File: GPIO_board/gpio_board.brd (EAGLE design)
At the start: 93.6 x 79 mm, 15 parts, among them J1 SWITCHES, J2 LED1, J3 LED2, Q1 IRF520, Q2 IRF520, Q3 IRF520, X1 PCI-E-164SLOT

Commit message: saving before autorouting
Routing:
- net N$24: track 2.54 -> 13.8 mm
- net N$23: track 2.54 -> 13.8 mm
- net N$22: track 2.54 -> 13.8 mm
- net N$21: track 2.54 -> 13.8 mm
- net N$17: track 2.54 -> 13.8 mm
- net N$16: track 2.54 -> 13.8 mm
- net N$15: track 2.54 -> 13.8 mm
- net N$14: track 2.54 -> 13.8 mm
- net N$20: track 2.54 -> 13.8 mm
- net N$19: track 2.54 -> 13.8 mm
- net N$18: track 2.54 -> 13.8 mm
- net N$13: track 29.0 -> 38.5 mm
- net N$25: track 28.2 -> 36.0 mm
- net N$26: track 27.5 -> 33.4 mm
- net N$27: track 26.8 -> 30.9 mm
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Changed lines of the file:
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@@
 <setting verticaltext="up"/>
 </settings>
-<grid distance="0.05" unitdist="inch" unit="inch" style="lines" multiple="1" display="yes" altdistance="0.005" altunitdist="inch" altunit="inch"/>
+<grid distance="0.005" unitdist="inch" unit="inch" style="lines" multiple="1" display="yes" altdistance="0.005" altunitdist="inch" altunit="inch"/>
 <layers>
 <layer number="1" name="Top" color="4" fill="1" visible="yes" active="yes"/>
@@
 <signal name="N$14">
 <contactref element="U$1" pad="23/A9"/>
-<wire x1="36.83" y1="43.18" x2="39.37" y2="43.18" width="0.4064" layer="1"/>
 <contactref element="U$2" pad="P$16"/>
-<wire x1="46.99" y1="52.07" x2="36.83" y2="43.18" width="0" layer="19" extent="1-1"/>
+<wire x1="36.83" y1="43.18" x2="38.1" y2="43.18" width="0.4064" layer="1"/>
+<wire x1="38.1" y1="43.18" x2="46.99" y2="52.07" width="0.4064" layer="1"/>
 </signal>
 <signal name="N$15">
 <contactref element="U$1" pad="22/A8"/>
-<wire x1="36.83" y1="40.64" x2="39.37" y2="40.64" width="0.4064" layer="1"/>
 <contactref element="U$2" pad="P$15"/>
-<wire x1="46.99" y1="49.53" x2="36.83" y2="40.64" width="0" layer="19" extent="1-1"/>
+<wire x1="36.83" y1="40.64" x2="38.1" y2="40.64" width="0.4064" layer="1"/>
+<wire x1="38.1" y1="40.64" x2="46.99" y2="49.53" width="0.4064" layer="1"/>
 </signal>
 <signal name="N$16">
 <contactref element="U$1" pad="21/A7"/>
-<wire x1="36.83" y1="38.1" x2="39.37" y2="38.1" width="0.4064" layer="1"/>
 <contactref element="U$2" pad="P$14"/>
-<wire x1="46.99" y1="46.99" x2="36.83" y2="38.1" width="0" layer="19" extent="1-1"/>
+<wire x1="46.99" y1="46.99" x2="38.1" y2="38.1" width="0.4064" layer="1"/>
+<wire x1="38.1" y1="38.1" x2="36.83" y2="38.1" width="0.4064" layer="1"/>
 </signal>
 <signal name="N$17">
 <contactref element="U$1" pad="20/A6"/>
-<wire x1="36.83" y1="35.56" x2="39.37" y2="35.56" width="0.4064" layer="1"/>
 <contactref element="U$2" pad="P$13"/>
-<wire x1="46.99" y1="44.45" x2="36.83" y2="35.56" width="0" layer="19" extent="1-1"/>
+<wire x1="36.83" y1="35.56" x2="38.1" y2="35.56" width="0.4064" layer="1"/>
+<wire x1="38.1" y1="35.56" x2="46.99" y2="44.45" width="0.4064" layer="1"/>
 </signal>
 <signal name="N$18">
 <contactref element="U$1" pad="19/A5"/>
-<wire x1="36.83" y1="33.02" x2="39.37" y2="33.02" width="0.4064" layer="1"/>
 <contactref element="U$2" pad="P$12"/>
-<wire x1="46.99" y1="41.91" x2="36.83" y2="33.02" width="0" layer="19" extent="1-1"/>
+<wire x1="36.83" y1="33.02" x2="38.1" y2="33.02" width="0.4064" layer="1"/>
+<wire x1="38.1" y1="33.02" x2="46.99" y2="41.91" width="0.4064" layer="1"/>
 </signal>
 <signal name="N$19">
 <contactref element="U$1" pad="18/A4"/>
-<wire x1="36.83" y1="30.48" x2="39.37" y2="30.48" width="0.4064" layer="1"/>
 <contactref element="U$2" pad="P$11"/>
-<wire x1="46.99" y1="39.37" x2="36.83" y2="30.48" width="0" layer="19" extent="1-1"/>
+<wire x1="36.83" y1="30.48" x2="38.1" y2="30.48" width="0.4064" layer="1"/>
+<wire x1="38.1" y1="30.48" x2="46.99" y2="39.37" width="0.4064" layer="1"/>
 </signal>
 <signal name="N$20">
 <contactref element="U$1" pad="17/A3"/>
-<wire x1="36.83" y1="27.94" x2="39.37" y2="27.94" width="0.4064" layer="1"/>
 <contactref element="U$2" pad="P$10"/>
-<wire x1="46.99" y1="36.83" x2="36.83" y2="27.94" width="0" layer="19" extent="1-1"/>
+<wire x1="36.83" y1="27.94" x2="38.1" y2="27.94" width="0.4064" layer="1"/>
+<wire x1="38.1" y1="27.94" x2="46.99" y2="36.83" width="0.4064" layer="1"/>
 </signal>
 <signal name="N$21">
 <contactref element="U$1" pad="16/A2"/>
-<wire x1="36.83" y1="25.4" x2="39.37" y2="25.4" width="0.4064" layer="1"/>
 <contactref element="U$2" pad="P$9"/>
-<wire x1="46.99" y1="34.29" x2="36.83" y2="25.4" width="0" layer="19" extent="1-1"/>
+<wire x1="36.83" y1="25.4" x2="38.1" y2="25.4" width="0.4064" layer="1"/>
+<wire x1="38.1" y1="25.4" x2="46.99" y2="34.29" width="0.4064" layer="1"/>
 </signal>
 <signal name="N$22">
 <contactref element="U$1" pad="15/A1"/>
-<wire x1="36.83" y1="22.86" x2="39.37" y2="22.86" width="0.4064" layer="1"/>
 <contactref element="U$2" pad="P$8"/>
-<wire x1="46.99" y1="31.75" x2="36.83" y2="22.86" width="0" layer="19" extent="1-1"/>
+<wire x1="36.83" y1="22.86" x2="38.1" y2="22.86" width="0.4064" layer="1"/>
+<wire x1="38.1" y1="22.86" x2="46.99" y2="31.75" width="0.4064" layer="1"/>
 </signal>
 <signal name="N$23">
 <contactref element="U$1" pad="14/A0"/>
-<wire x1="36.83" y1="20.32" x2="39.37" y2="20.32" width="0.4064" layer="1"/>
 <contactref element="U$2" pad="P$7"/>
-<wire x1="46.99" y1="29.21" x2="36.83" y2="20.32" width="0" layer="19" extent="1-1"/>
+<wire x1="36.83" y1="20.32" x2="38.1" y2="20.32" width="0.4064" layer="1"/>
+<wire x1="38.1" y1="20.32" x2="46.99" y2="29.21" width="0.4064" layer="1"/>
 </signal>
 <signal name="N$24">
 <contactref element="U$1" pad="13"/>
-<wire x1="36.83" y1="17.78" x2="39.37" y2="17.78" width="0.4064" layer="1"/>
 <contactref element="U$2" pad="P$6"/>
-<wire x1="46.99" y1="26.67" x2="36.83" y2="17.78" width="0" layer="19" extent="1-1"/>
+<wire x1="36.83" y1="17.78" x2="38.1" y2="17.78" width="0.4064" layer="1"/>
+<wire x1="38.1" y1="17.78" x2="46.99" y2="26.67" width="0.4064" layer="1"/>
 </signal>
 <signal name="N$13">
 <contactref element="U$1" pad="8"/>
+<contactref element="U$2" pad="P$5"/>
 <wire x1="21.59" y1="27.94" x2="33.02" y2="27.94" width="0.4064" layer="1"/>
 <wire x1="33.02" y1="27.94" x2="34.29" y2="26.67" width="0.4064" layer="1"/>
-<wire x1="34.29" y1="26.67" x2="34.29" y2="16.51" width="0.4064" layer="1"/>
-<wire x1="34.29" y1="16.51" x2="35.56" y2="15.24" width="0.4064" layer="1"/>
-<wire x1="35.56" y1="15.24" x2="39.37" y2="15.24" width="0.4064" layer="1"/>
-<contactref element="U$2" pad="P$5"/>
-<wire x1="46.99" y1="24.13" x2="34.29" y2="16.51" width="0" layer="19" extent="1-1"/>
+<wire x1="34.29" y1="26.67" x2="34.29" y2="17.78" width="0.4064" layer="1"/>
+<wire x1="34.29" y1="17.78" x2="35.56" y2="16.51" width="0.4064" layer="1"/>
+<wire x1="35.56" y1="16.51" x2="39.37" y2="16.51" width="0.4064" layer="1"/>
+<wire x1="39.37" y1="16.51" x2="46.99" y2="24.13" width="0.4064" layer="1"/>
 </signal>
 <signal name="N$25">
 <contactref element="U$1" pad="9"/>
+<contactref element="U$2" pad="P$4"/>
 <wire x1="21.59" y1="25.4" x2="31.75" y2="25.4" width="0.4064" layer="1"/>
 <wire x1="31.75" y1="25.4" x2="33.02" y2="24.13" width="0.4064" layer="1"/>
-<wire x1="33.02" y1="24.13" x2="33.02" y2="16.51" width="0.4064" layer="1"/>
-<wire x1="33.02" y1="16.51" x2="35.56" y2="13.97" width="0.4064" layer="1"/>
-<wire x1="35.56" y1="13.97" x2="40.64" y2="13.97" width="0.4064" layer="1"/>
-<contactref element="U$2" pad="P$4"/>
-<wire x1="46.99" y1="21.59" x2="21.59" y2="25.4" width="0" layer="19" extent="1-1"/>
+<wire x1="33.02" y1="24.13" x2="33.02" y2="17.78" width="0.4064" layer="1"/>
+<wire x1="33.02" y1="17.78" x2="35.56" y2="15.24" width="0.4064" layer="1"/>
+<wire x1="35.56" y1="15.24" x2="40.64" y2="15.24" width="0.4064" layer="1"/>
+<wire x1="40.64" y1="15.24" x2="46.99" y2="21.59" width="0.4064" layer="1"/>
 </signal>
 <signal name="N$26">
 <contactref element="U$1" pad="10"/>
+<contactref element="U$2" pad="P$3"/>
 <wire x1="21.59" y1="22.86" x2="30.48" y2="22.86" width="0.4064" layer="1"/>
 <wire x1="30.48" y1="22.86" x2="31.75" y2="21.59" width="0.4064" layer="1"/>
-<wire x1="31.75" y1="21.59" x2="31.75" y2="16.51" width="0.4064" layer="1"/>
-<wire x1="31.75" y1="16.51" x2="35.56" y2="12.7" width="0.4064" layer="1"/>
-<wire x1="35.56" y1="12.7" x2="41.91" y2="12.7" width="0.4064" layer="1"/>
-<contactref element="U$2" pad="P$3"/>
-<wire x1="46.99" y1="19.05" x2="21.59" y2="22.86" width="0" layer="19" extent="1-1"/>
+<wire x1="31.75" y1="21.59" x2="31.75" y2="17.78" width="0.4064" layer="1"/>
+<wire x1="31.75" y1="17.78" x2="35.56" y2="13.97" width="0.4064" layer="1"/>
+<wire x1="35.56" y1="13.97" x2="41.91" y2="13.97" width="0.4064" layer="1"/>
+<wire x1="41.91" y1="13.97" x2="46.99" y2="19.05" width="0.4064" layer="1"/>
 </signal>
 <signal name="N$27">
 <contactref element="U$1" pad="11"/>
+<contactref element="U$2" pad="P$2"/>
 <wire x1="21.59" y1="20.32" x2="29.21" y2="20.32" width="0.4064" layer="1"/>
 <wire x1="29.21" y1="20.32" x2="30.48" y2="19.05" width="0.4064" layer="1"/>
-<wire x1="30.48" y1="19.05" x2="30.48" y2="16.51" width="0.4064" layer="1"/>
-<wire x1="30.48" y1="16.51" x2="35.56" y2="11.43" width="0.4064" layer="1"/>
-<wire x1="35.56" y1="11.43" x2="43.18" y2="11.43" width="0.4064" layer="1"/>
-<contactref element="U$2" pad="P$2"/>
-<wire x1="46.99" y1="16.51" x2="21.59" y2="20.32" width="0" layer="19" extent="1-1"/>
+<wire x1="30.48" y1="19.05" x2="30.48" y2="17.78" width="0.4064" layer="1"/>
+<wire x1="30.48" y1="17.78" x2="35.56" y2="12.7" width="0.4064" layer="1"/>
+<wire x1="35.56" y1="12.7" x2="43.18" y2="12.7" width="0.4064" layer="1"/>
+<wire x1="43.18" y1="12.7" x2="46.99" y2="16.51" width="0.4064" layer="1"/>
 </signal>
 <signal name="N$28">
 <contactref element="U$1" pad="12"/>
-<wire x1="21.59" y1="17.78" x2="27.94" y2="17.78" width="0.4064" layer="1"/>
-<wire x1="27.94" y1="17.78" x2="35.56" y2="10.16" width="0.4064" layer="1"/>
-<wire x1="35.56" y1="10.16" x2="44.45" y2="10.16" width="0.4064" layer="1"/>
 <contactref element="U$2" pad="P$1"/>
-<wire x1="46.99" y1="13.97" x2="21.59" y2="17.78" width="0" layer="19" extent="1-1"/>
+<wire x1="21.59" y1="17.78" x2="29.21" y2="17.78" width="0.4064" layer="1"/>
+<wire x1="29.21" y1="17.78" x2="35.56" y2="11.43" width="0.4064" layer="1"/>
+<wire x1="35.56" y1="11.43" x2="44.45" y2="11.43" width="0.4064" layer="1"/>
+<wire x1="44.45" y1="11.43" x2="46.99" y2="13.97" width="0.4064" layer="1"/>
 </signal>
 <signal name="N$29">

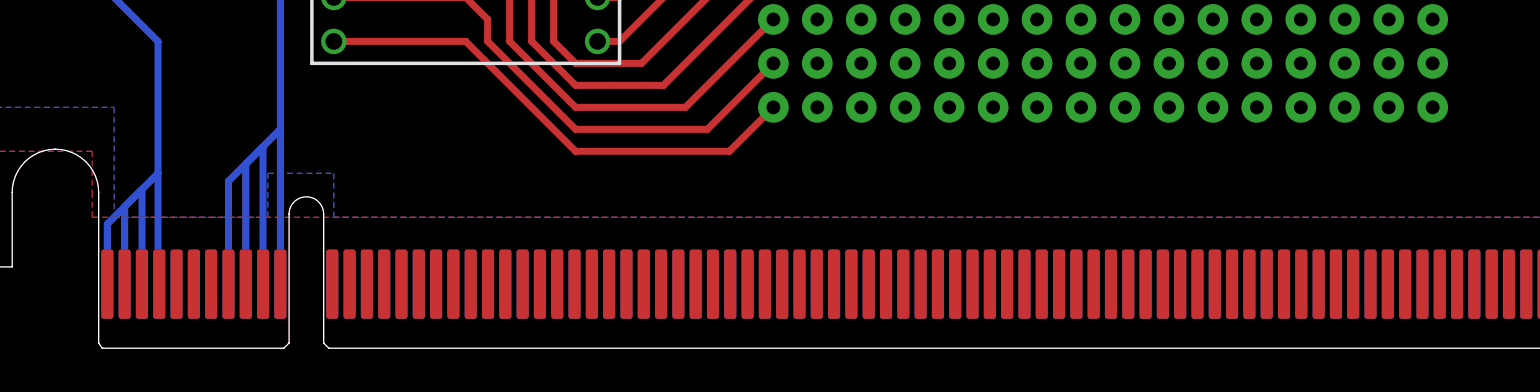
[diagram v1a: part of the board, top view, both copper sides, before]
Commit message: fixed traces from PCIe slot to proto_grid
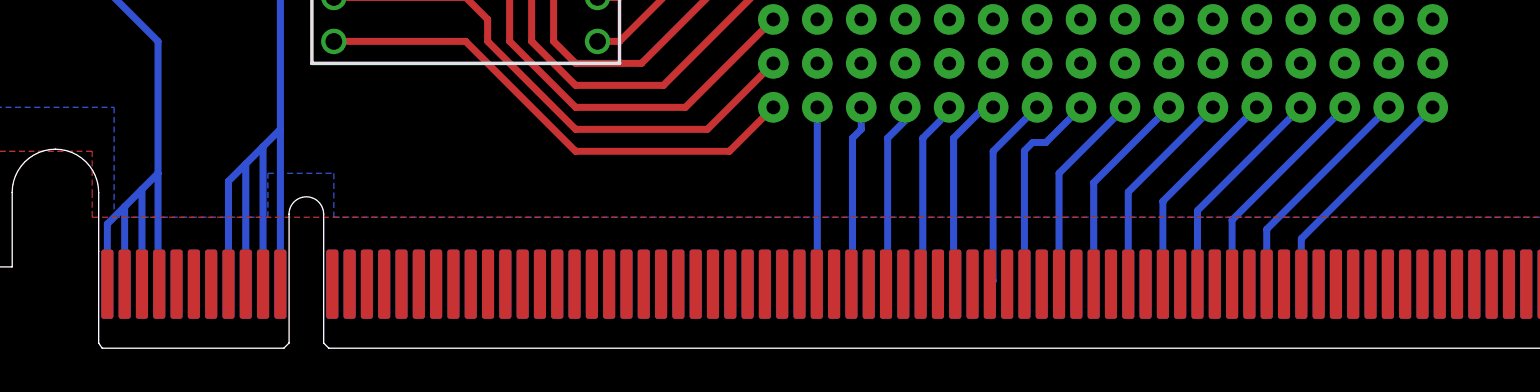
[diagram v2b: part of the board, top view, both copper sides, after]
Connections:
- net N$29: now also X1.A68; no longer X1.A54
- net N$30: now also X1.A66; no longer X1.A53
- net N$31: now also X1.A64; no longer X1.A52
- net N$32: now also X1.A62; no longer X1.A51
- net N$33: now also X1.A60; no longer X1.A50
- net N$34: now also X1.A58; no longer X1.A49
- net N$35: now also X1.A56; no longer X1.A48
- net N$36: now also X1.A54; no longer X1.A47
- net N$37: now also X1.A52; no longer X1.A46
- net N$38: now also X1.A50; no longer X1.A45
- net N$39: now also X1.A48; no longer X1.A44
- net N$40: now also X1.A46; no longer X1.A43
- net N$41: now also X1.A44; no longer X1.A42
- net N$42: now also X1.A42; no longer X1.A41
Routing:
- net N$29: track 0.00 -> 13.4 mm
- net N$30: track 0.00 -> 13.1 mm
- net N$31: track 0.00 -> 12.9 mm
- net N$32: track 0.00 -> 12.7 mm
- net N$33: track 0.00 -> 12.5 mm
- net N$34: track 0.00 -> 12.2 mm
- net N$35: track 0.00 -> 12.0 mm
- net N$37: track 0.00 -> 12.0 mm
- net N$36: track 0.00 -> 11.8 mm
- net N$39: track 0.00 -> 11.5 mm
- net N$38: track 0.00 -> 11.4 mm
- net N$40: track 0.00 -> 10.9 mm
- net N$41: track 0.00 -> 10.7 mm
- net N$42: track 0.00 -> 10.5 mm
- net N$43: track 0.00 -> 10.2 mm
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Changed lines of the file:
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@@
 <setting verticaltext="up"/>
 </settings>
-<grid distance="0.005" unitdist="inch" unit="inch" style="lines" multiple="1" display="yes" altdistance="0.005" altunitdist="inch" altunit="inch"/>
+<grid distance="0.01" unitdist="inch" unit="inch" style="lines" multiple="1" display="yes" altdistance="0.005" altunitdist="inch" altunit="inch"/>
 <layers>
 <layer number="1" name="Top" color="4" fill="1" visible="yes" active="yes"/>
@@
 <wire x1="17.78" y1="46.99" x2="21.59" y2="50.8" width="0.4064" layer="16"/>
 <wire x1="17.5" y1="3.75" x2="17.5" y2="11.7" width="0.4064" layer="16"/>
-<wire x1="17.5" y1="11.7" x2="18.14" y2="12.34" width="0.4064" layer="16"/>
-<wire x1="18.14" y1="12.34" x2="18.5" y2="12.7" width="0.4064" layer="16"/>
+<wire x1="17.5" y1="11.7" x2="18.5" y2="12.7" width="0.4064" layer="16"/>
 <wire x1="16.5" y1="3.75" x2="16.5" y2="10.7" width="0.4064" layer="16"/>
 <wire x1="16.5" y1="10.7" x2="17.5" y2="11.7" width="0.4064" layer="16"/>
 <wire x1="15.5" y1="3.75" x2="15.5" y2="9.7" width="0.4064" layer="16"/>
-<wire x1="15.5" y1="9.7" x2="17.5" y2="11.7" width="0.4064" layer="16"/>
+<wire x1="15.5" y1="9.7" x2="16.5" y2="10.7" width="0.4064" layer="16"/>
 <polygon width="0.4064" layer="1">
 <vertex x="-1.27" y="83.82"/>
@@
 <wire x1="9.5" y1="8.23" x2="10.5" y2="9.23" width="0.4064" layer="16"/>
 <wire x1="8.5" y1="3.75" x2="8.5" y2="7.23" width="0.4064" layer="16"/>
-<wire x1="8.5" y1="7.23" x2="10.5" y2="9.23" width="0.4064" layer="16"/>
+<wire x1="8.5" y1="7.23" x2="9.5" y2="8.23" width="0.4064" layer="16"/>
 </signal>
 <signal name="N$9">
@@
 <signal name="N$29">
 <contactref element="U$2" pad="P$225"/>
-<contactref element="X1" pad="A54"/>
-<wire x1="63.5" y1="3.75" x2="85.09" y2="13.97" width="0" layer="19" extent="16-16"/>
+<contactref element="X1" pad="A68"/>
+<wire x1="77.5" y1="3.75" x2="77.5" y2="6.38" width="0.4064" layer="16"/>
+<wire x1="77.5" y1="6.38" x2="85.09" y2="13.97" width="0.4064" layer="16"/>
 </signal>
 <signal name="N$30">
 <contactref element="U$2" pad="P$233"/>
-<contactref element="X1" pad="A53"/>
-<wire x1="62.5" y1="3.75" x2="82.55" y2="13.97" width="0" layer="19" extent="16-16"/>
+<contactref element="X1" pad="A66"/>
+<wire x1="75.5" y1="3.75" x2="75.5" y2="6.92" width="0.4064" layer="16"/>
+<wire x1="75.5" y1="6.92" x2="82.55" y2="13.97" width="0.4064" layer="16"/>
 </signal>
 <signal name="N$31">
 <contactref element="U$2" pad="P$193"/>
-<contactref element="X1" pad="A52"/>
-<wire x1="61.5" y1="3.75" x2="80.01" y2="13.97" width="0" layer="19" extent="16-16"/>
+<contactref element="X1" pad="A64"/>
+<wire x1="73.5" y1="3.75" x2="73.5" y2="7.46" width="0.4064" layer="16"/>
+<wire x1="73.5" y1="7.46" x2="80.01" y2="13.97" width="0.4064" layer="16"/>
 </signal>
 <signal name="N$32">
 <contactref element="U$2" pad="P$201"/>
-<contactref element="X1" pad="A51"/>
-<wire x1="60.5" y1="3.75" x2="77.47" y2="13.97" width="0" layer="19" extent="16-16"/>
+<contactref element="X1" pad="A62"/>
+<wire x1="71.5" y1="3.75" x2="71.5" y2="8" width="0.4064" layer="16"/>
+<wire x1="71.5" y1="8" x2="77.47" y2="13.97" width="0.4064" layer="16"/>
 </signal>
 <signal name="N$33">
 <contactref element="U$2" pad="P$161"/>
-<contactref element="X1" pad="A50"/>
-<wire x1="59.5" y1="3.75" x2="74.93" y2="13.97" width="0" layer="19" extent="16-16"/>
+<contactref element="X1" pad="A60"/>
+<wire x1="69.5" y1="3.75" x2="69.5" y2="8.54" width="0.4064" layer="16"/>
+<wire x1="69.5" y1="8.54" x2="74.93" y2="13.97" width="0.4064" layer="16"/>
 </signal>
 <signal name="N$34">
 <contactref element="U$2" pad="P$169"/>
-<contactref element="X1" pad="A49"/>
-<wire x1="58.5" y1="3.75" x2="72.39" y2="13.97" width="0" layer="19" extent="16-16"/>
+<contactref element="X1" pad="A58"/>
+<wire x1="67.5" y1="3.75" x2="67.5" y2="9.08" width="0.4064" layer="16"/>
+<wire x1="67.5" y1="9.08" x2="72.39" y2="13.97" width="0.4064" layer="16"/>
 </signal>
 <signal name="N$35">
 <contactref element="U$2" pad="P$129"/>
-<contactref element="X1" pad="A48"/>
-<wire x1="57.5" y1="3.75" x2="69.85" y2="13.97" width="0" layer="19" extent="16-16"/>
+<contactref element="X1" pad="A56"/>
+<wire x1="65.5" y1="3.75" x2="65.5" y2="9.62" width="0.4064" layer="16"/>
+<wire x1="65.5" y1="9.62" x2="69.85" y2="13.97" width="0.4064" layer="16"/>
 </signal>
 <signal name="N$36">
 <contactref element="U$2" pad="P$137"/>
-<contactref element="X1" pad="A47"/>
-<wire x1="56.5" y1="3.75" x2="67.31" y2="13.97" width="0" layer="19" extent="16-16"/>
+<contactref element="X1" pad="A54"/>
+<wire x1="63.5" y1="3.75" x2="63.5" y2="10.16" width="0.4064" layer="16"/>
+<wire x1="63.5" y1="10.16" x2="67.31" y2="13.97" width="0.4064" layer="16"/>
 </signal>
 <signal name="N$37">
 <contactref element="U$2" pad="P$97"/>
-<contactref element="X1" pad="A46"/>
-<wire x1="55.5" y1="3.75" x2="64.77" y2="13.97" width="0" layer="19" extent="16-16"/>
+<contactref element="X1" pad="A52"/>
+<wire x1="61.5" y1="3.75" x2="61.5" y2="11.462" width="0.4064" layer="16"/>
+<wire x1="61.5" y1="11.462" x2="61.976" y2="11.938" width="0.4064" layer="16"/>
+<wire x1="61.976" y1="11.938" x2="62.738" y2="11.938" width="0.4064" layer="16"/>
+<wire x1="62.738" y1="11.938" x2="64.77" y2="13.97" width="0.4064" layer="16"/>
 </signal>
 <signal name="N$38">
 <contactref element="U$2" pad="P$105"/>
-<contactref element="X1" pad="A45"/>
-<wire x1="54.5" y1="3.75" x2="62.23" y2="13.97" width="0" layer="19" extent="16-16"/>
+<contactref element="X1" pad="A50"/>
+<wire x1="62.23" y1="13.97" x2="59.69" y2="11.43" width="0.4064" layer="16"/>
+<wire x1="59.69" y1="11.43" x2="59.69" y2="3.94" width="0.4064" layer="16"/>
+<wire x1="59.69" y1="3.94" x2="59.5" y2="3.75" width="0.4064" layer="16"/>
 </signal>
 <signal name="N$39">
 <contactref element="U$2" pad="P$65"/>
-<contactref element="X1" pad="A44"/>
-<wire x1="53.5" y1="3.75" x2="59.69" y2="13.97" width="0" layer="19" extent="16-16"/>
+<contactref element="X1" pad="A48"/>
+<wire x1="59.69" y1="13.97" x2="59.182" y2="13.97" width="0.4064" layer="16"/>
+<wire x1="59.182" y1="13.97" x2="57.404" y2="12.192" width="0.4064" layer="16"/>
+<wire x1="57.404" y1="12.192" x2="57.404" y2="3.846" width="0.4064" layer="16"/>
+<wire x1="57.404" y1="3.846" x2="57.5" y2="3.75" width="0.4064" layer="16"/>
 </signal>
 <signal name="N$40">
 <contactref element="U$2" pad="P$73"/>
-<contactref element="X1" pad="A43"/>
-<wire x1="52.5" y1="3.75" x2="57.15" y2="13.97" width="0" layer="19" extent="16-16"/>
+<contactref element="X1" pad="A46"/>
+<wire x1="57.15" y1="13.97" x2="57.15" y2="13.716" width="0.4064" layer="16"/>
+<wire x1="57.15" y1="13.716" x2="55.626" y2="12.192" width="0.4064" layer="16"/>
+<wire x1="55.626" y1="12.192" x2="55.626" y2="3.876" width="0.4064" layer="16"/>
+<wire x1="55.626" y1="3.876" x2="55.5" y2="3.75" width="0.4064" layer="16"/>
 </signal>
 <signal name="N$41">
 <contactref element="U$2" pad="P$33"/>
-<contactref element="X1" pad="A42"/>
-<wire x1="51.5" y1="3.75" x2="54.61" y2="13.97" width="0" layer="19" extent="16-16"/>
+<contactref element="X1" pad="A44"/>
+<wire x1="54.61" y1="13.97" x2="54.61" y2="13.208" width="0.4064" layer="16"/>
+<wire x1="54.61" y1="13.208" x2="53.594" y2="12.192" width="0.4064" layer="16"/>
+<wire x1="53.594" y1="12.192" x2="53.594" y2="3.844" width="0.4064" layer="16"/>
+<wire x1="53.594" y1="3.844" x2="53.5" y2="3.75" width="0.4064" layer="16"/>
 </signal>
 <signal name="N$42">
 <contactref element="U$2" pad="P$41"/>
-<contactref element="X1" pad="A41"/>
-<wire x1="50.5" y1="3.75" x2="52.07" y2="13.97" width="0" layer="19" extent="16-16"/>
+<contactref element="X1" pad="A42"/>
+<wire x1="52.07" y1="13.97" x2="52.07" y2="12.7" width="0.4064" layer="16"/>
+<wire x1="52.07" y1="12.7" x2="51.562" y2="12.192" width="0.4064" layer="16"/>
+<wire x1="51.562" y1="12.192" x2="51.562" y2="3.812" width="0.4064" layer="16"/>
+<wire x1="51.562" y1="3.812" x2="51.5" y2="3.75" width="0.4064" layer="16"/>
 </signal>
 <signal name="N$43">
 <contactref element="U$2" pad="P$17"/>
 <contactref element="X1" pad="A40"/>
-<wire x1="49.5" y1="3.75" x2="49.53" y2="13.97" width="0" layer="19" extent="16-16"/>
+<wire x1="49.53" y1="13.97" x2="49.53" y2="3.78" width="0.4064" layer="16"/>
+<wire x1="49.53" y1="3.78" x2="49.5" y2="3.75" width="0.4064" layer="16"/>
 </signal>
 </signals>
